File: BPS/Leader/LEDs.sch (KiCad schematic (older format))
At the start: 16 parts

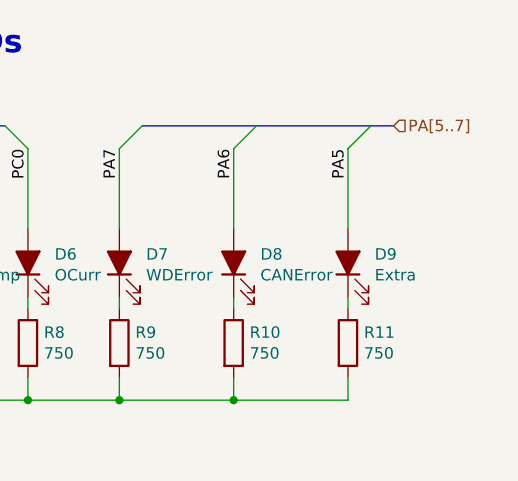
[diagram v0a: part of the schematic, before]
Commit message: Places most components of leader board in their respective locations with nothing traced
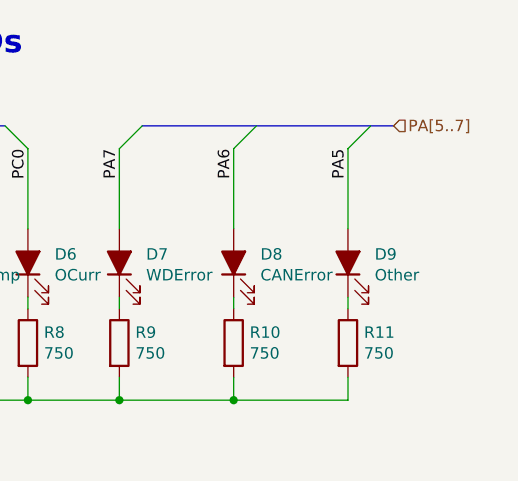
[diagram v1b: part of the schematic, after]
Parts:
- D9: value Extra -> Other
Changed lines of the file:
@@
 P 6300 3100
 F 0 "D9" V 6338 2983 50  0000 R CNN
-F 1 "Extra" V 6247 2983 50  0000 R CNN
+F 1 "Other" V 6247 2983 50  0000 R CNN
 F 2 "LED_SMD:LED_0805_2012Metric" H 6300 3100 50  0001 C CNN
 F 3 "~" H 6300 3100 50  0001 C CNN

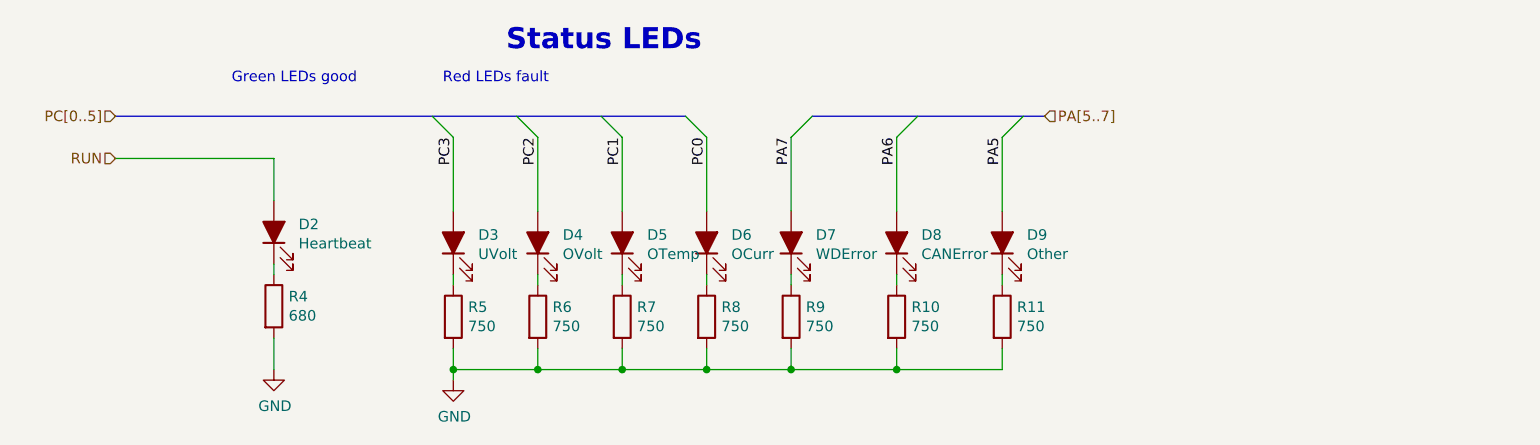
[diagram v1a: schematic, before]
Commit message: Adds power planes
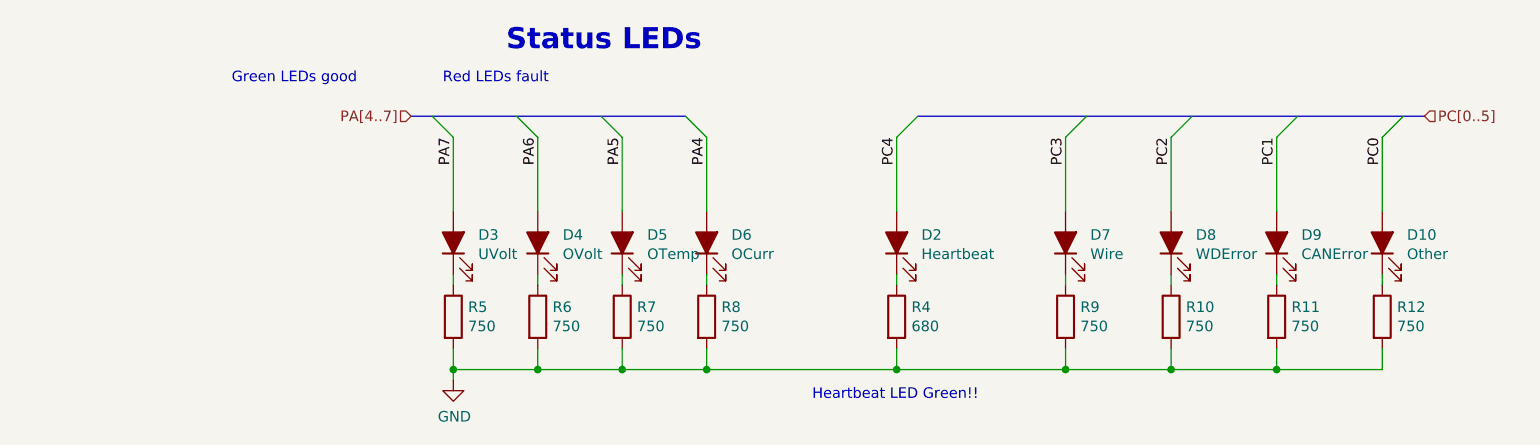
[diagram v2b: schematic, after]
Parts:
- added D10: Other, LED_SMD:LED_0805_2012Metric, symbol Device:LED_ALT
- added R12: 750, Resistor_SMD:R_0805_2012Metric, symbol Device:R
- D7: value WDError -> Wire
- D8: value CANError -> WDError
- D9: value Other -> CANError
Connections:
- net GND: now also R12.2
- net PA5: now also D5.2 (A); no longer D9.2 (A)
- net PA6: now also D4.2 (A); no longer D8.2 (A)
- net PA7: now also D3.2 (A); no longer D7.2 (A)
- net PC0: now also D10.2 (A); no longer D6.2 (A)
- net PC1: now also D9.2 (A); no longer D5.2 (A)
- net PC2: now also D8.2 (A); no longer D4.2 (A)
- net PC3: now also D7.2 (A); no longer D3.2 (A)
- net RUN renamed PC4
- new net: D10.1 (K), R12.1
- new net PA4: D6.2 (A)
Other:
- note added: "Heartbeat LED Green!!"
- moved on the sheet: D2, D7, D8, D9, R10, R11, R4, R9
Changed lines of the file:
@@
 Comment4 ""
 $EndDescr
-Text HLabel 2100 2500 0    50   Input ~ 0
+Text HLabel 8300 2500 2    50   Input ~ 0
 PC[0..5]
 $Comp
 L Device:LED_ALT D2
 U 1 1 5C3C069F
-P 2850 3050
-F 0 "D2" V 2888 2933 50  0000 R CNN
-F 1 "Heartbeat" V 2797 2933 50  0000 R CNN
-F 2 "LED_SMD:LED_0805_2012Metric" H 2850 3050 50  0001 C CNN
-F 3 "~" H 2850 3050 50  0001 C CNN
-F 4 "Green" V 2850 3050 50  0001 C CNN "Color"
-F 5 "APTD2012LCGCK" V 2850 3050 50  0001 C CNN "P/N"
-	1    2850 3050
+P 5800 3100
+F 0 "D2" V 5838 2983 50  0000 R CNN
+F 1 "Heartbeat" V 5747 2983 50  0000 R CNN
+F 2 "LED_SMD:LED_0805_2012Metric" H 5800 3100 50  0001 C CNN
+F 3 "~" H 5800 3100 50  0001 C CNN
+F 4 "Green" V 5800 3100 50  0001 C CNN "Color"
+F 5 "APTD2012LCGCK" V 5800 3100 50  0001 C CNN "P/N"
+	1    5800 3100
 	0    -1   -1   0
 $EndComp
@@
 	0    -1   -1   0
 $EndComp
-$Comp
-L power:GND #PWR033
-U 1 1 5C3C06CA
-P 2850 3700
-F 0 "#PWR033" H 2850 3450 50  0001 C CNN
-F 1 "GND" H 2855 3527 50  0000 C CNN
-F 2 "" H 2850 3700 50  0001 C CNN
-F 3 "" H 2850 3700 50  0001 C CNN
-	1    2850 3700
-	1    0    0    -1
-$EndComp
 Wire Wire Line
 	4900 3700 4900 3600
@@
 L Device:R R4
 U 1 1 5C3C06D9
-P 2850 3400
-F 0 "R4" H 2920 3446 50  0000 L CNN
-F 1 "680" H 2920 3355 50  0000 L CNN
-F 2 "Resistor_SMD:R_0805_2012Metric" V 2780 3400 50  0001 C CNN
-F 3 "~" H 2850 3400 50  0001 C CNN
-	1    2850 3400
+P 5800 3450
+F 0 "R4" H 5870 3496 50  0000 L CNN
+F 1 "680" H 5870 3405 50  0000 L CNN
+F 2 "Resistor_SMD:R_0805_2012Metric" V 5730 3450 50  0001 C CNN
+F 3 "~" H 5800 3450 50  0001 C CNN
+	1    5800 3450
 	1    0    0    -1
 $EndComp
@@
 	3700 3250 3700 3300
 Wire Wire Line
-	2850 3200 2850 3250
-Wire Wire Line
-	3700 2950 3700 2600
-Wire Wire Line
-	4100 2950 4100 2600
-Wire Wire Line
-	4500 2950 4500 2600
-Wire Wire Line
-	4900 2950 4900 2600
-Text Label 3700 2600 3    50   ~ 0
+	5800 3250 5800 3300
+Wire Wire Line
+	8100 2950 8100 2600
+Wire Wire Line
+	7600 2950 7600 2600
+Wire Wire Line
+	7100 2950 7100 2600
+Wire Wire Line
+	6600 2950 6600 2600
+Text Label 6600 2600 3    50   ~ 0
 PC3
-Text Label 4100 2600 3    50   ~ 0
+Text Label 7100 2600 3    50   ~ 0
 PC2
-Text Label 4500 2600 3    50   ~ 0
+Text Label 7600 2600 3    50   ~ 0
 PC1
-Text Label 4900 2600 3    50   ~ 0
+Text Label 8100 2600 3    50   ~ 0
 PC0
 Connection ~ 3700 3700
 Text Notes 2650 2350 0    50   ~ 0
 Green LEDs good
-$Comp
-L Device:LED_ALT D7
-U 1 1 5C3C070F
-P 5300 3100
-F 0 "D7" V 5338 2983 50  0000 R CNN
-F 1 "WDError" V 5247 2983 50  0000 R CNN
-F 2 "LED_SMD:LED_0805_2012Metric" H 5300 3100 50  0001 C CNN
-F 3 "~" H 5300 3100 50  0001 C CNN
-F 4 "Red" V 5300 3100 50  0001 C CNN "Color"
-F 5 "APTD2012LSURCK" V 5300 3100 50  0001 C CNN "P/N"
-	1    5300 3100
-	0    -1   -1   0
-$EndComp
-Wire Wire Line
-	5300 3700 5300 3600
-Wire Wire Line
-	4900 3700 5300 3700
+Wire Wire Line
+	6600 3700 6600 3600
 $Comp
 L Device:R R9
 U 1 1 5C3C0718
-P 5300 3450
-F 0 "R9" H 5370 3496 50  0000 L CNN
-F 1 "750" H 5370 3405 50  0000 L CNN
-F 2 "Resistor_SMD:R_0805_2012Metric" V 5230 3450 50  0001 C CNN
-F 3 "~" H 5300 3450 50  0001 C CNN
-	1    5300 3450
-	1    0    0    -1
-$EndComp
-Wire Wire Line
-	5300 3250 5300 3300
-Wire Wire Line
-	5300 2950 5300 2600
-Wire Wire Line
-	2850 3550 2850 3700
+P 6600 3450
+F 0 "R9" H 6670 3496 50  0000 L CNN
+F 1 "750" H 6670 3405 50  0000 L CNN
+F 2 "Resistor_SMD:R_0805_2012Metric" V 6530 3450 50  0001 C CNN
+F 3 "~" H 6600 3450 50  0001 C CNN
+	1    6600 3450
+	1    0    0    -1
+$EndComp
+Wire Wire Line
+	6600 3250 6600 3300
+Wire Wire Line
+	4900 2950 4900 2600
+Wire Wire Line
+	5800 3600 5800 3700
 $Comp
 L power:GND #PWR034
@@
 Text Notes 3650 2350 0    50   ~ 0
 Red LEDs fault
-Connection ~ 4900 3700
 Text Notes 3950 2200 0    100  ~ 20
 Status LEDs
 Entry Wire Line
-	3600 2500 3700 2600
-Entry Wire Line
-	4000 2500 4100 2600
-Entry Wire Line
-	4400 2500 4500 2600
-Entry Wire Line
-	4800 2500 4900 2600
+	8200 2500 8100 2600
+Entry Wire Line
+	7700 2500 7600 2600
+Entry Wire Line
+	7200 2500 7100 2600
+Entry Wire Line
+	6700 2500 6600 2600
+Wire Wire Line
+	7100 3700 7100 3600
+$Comp
+L Device:R R10
+U 1 1 5C6CF943
+P 7100 3450
+F 0 "R10" H 7170 3496 50  0000 L CNN
+F 1 "750" H 7170 3405 50  0000 L CNN
+F 2 "Resistor_SMD:R_0805_2012Metric" V 7030 3450 50  0001 C CNN
+F 3 "~" H 7100 3450 50  0001 C CNN
+	1    7100 3450
+	1    0    0    -1
+$EndComp
+Wire Wire Line
+	7100 3250 7100 3300
+Wire Wire Line
+	4500 2950 4500 2600
+Wire Wire Line
+	6600 3700 7100 3700
+Connection ~ 6600 3700
+Entry Wire Line
+	4900 2600 4800 2500
+Entry Wire Line
+	4500 2600 4400 2500
+Text Label 4500 2600 3    50   ~ 0
+PA5
+Text Label 4100 2600 3    50   ~ 0
+PA6
+Text HLabel 3500 2500 0    50   Input ~ 0
+PA[4..7]
+Wire Wire Line
+	7600 3700 7600 3600
+$Comp
+L Device:R R11
+U 1 1 5C585DC3
+P 7600 3450
+F 0 "R11" H 7670 3496 50  0000 L CNN
+F 1 "750" H 7670 3405 50  0000 L CNN
+F 2 "Resistor_SMD:R_0805_2012Metric" V 7530 3450 50  0001 C CNN
+F 3 "~" H 7600 3450 50  0001 C CNN
+	1    7600 3450
+	1    0    0    -1
+$EndComp
+Wire Wire Line
+	7600 3250 7600 3300
+Wire Wire Line
+	4100 2950 4100 2600
+Wire Wire Line
+	7100 3700 7600 3700
+Entry Wire Line
+	4100 2600 4000 2500
+Text Label 3700 2600 3    50   ~ 0
+PA7
+Wire Wire Line
+	5800 2950 5800 2600
+Connection ~ 7100 3700
+$Comp
+L Device:LED_ALT D10
+U 1 1 5F16CED0
+P 8100 3100
+F 0 "D10" V 8138 2983 50  0000 R CNN
+F 1 "Other" V 8047 2983 50  0000 R CNN
+F 2 "LED_SMD:LED_0805_2012Metric" H 8100 3100 50  0001 C CNN
+F 3 "~" H 8100 3100 50  0001 C CNN
+F 4 "Red" V 8100 3100 50  0001 C CNN "Color"
+F 5 "APTD2012LSURCK" V 8100 3100 50  0001 C CNN "P/N"
+	1    8100 3100
+	0    -1   -1   0
+$EndComp
+$Comp
+L Device:R R12
+U 1 1 5F16CED6
+P 8100 3450
+F 0 "R12" H 8170 3496 50  0000 L CNN
+F 1 "750" H 8170 3405 50  0000 L CNN
+F 2 "Resistor_SMD:R_0805_2012Metric" V 8030 3450 50  0001 C CNN
+F 3 "~" H 8100 3450 50  0001 C CNN
+	1    8100 3450
+	1    0    0    -1
+$EndComp
+Wire Wire Line
+	8100 3250 8100 3300
+Wire Wire Line
+	3700 2950 3700 2600
+Entry Wire Line
+	3700 2600 3600 2500
+Text Label 4900 2600 3    50   ~ 0
+PA4
+Wire Wire Line
+	8100 3700 8100 3600
+Connection ~ 7600 3700
+Wire Wire Line
+	7600 3700 8100 3700
+$Comp
+L Device:LED_ALT D7
+U 1 1 5C3C070F
+P 6600 3100
+F 0 "D7" V 6638 2983 50  0000 R CNN
+F 1 "Wire" V 6547 2983 50  0000 R CNN
+F 2 "LED_SMD:LED_0805_2012Metric" H 6600 3100 50  0001 C CNN
+F 3 "~" H 6600 3100 50  0001 C CNN
+F 4 "Red" V 6600 3100 50  0001 C CNN "Color"
+F 5 "APTD2012LSURCK" V 6600 3100 50  0001 C CNN "P/N"
+	1    6600 3100
+	0    -1   -1   0
+$EndComp
 $Comp
 L Device:LED_ALT D8
 U 1 1 5C6CF93B
-P 5800 3100
-F 0 "D8" V 5838 2983 50  0000 R CNN
-F 1 "CANError" V 5747 2983 50  0000 R CNN
-F 2 "LED_SMD:LED_0805_2012Metric" H 5800 3100 50  0001 C CNN
-F 3 "~" H 5800 3100 50  0001 C CNN
-F 4 "Red" V 5800 3100 50  0001 C CNN "Color"
-F 5 "APTD2012LSURCK" V 5800 3100 50  0001 C CNN "P/N"
-	1    5800 3100
-	0    -1   -1   0
-$EndComp
-Wire Wire Line
-	5800 3700 5800 3600
-$Comp
-L Device:R R10
-U 1 1 5C6CF943
-P 5800 3450
-F 0 "R10" H 5870 3496 50  0000 L CNN
-F 1 "750" H 5870 3405 50  0000 L CNN
-F 2 "Resistor_SMD:R_0805_2012Metric" V 5730 3450 50  0001 C CNN
-F 3 "~" H 5800 3450 50  0001 C CNN
-	1    5800 3450
-	1    0    0    -1
-$EndComp
-Wire Wire Line
-	5800 3250 5800 3300
-Wire Wire Line
-	5800 2950 5800 2600
-Wire Wire Line
-	5300 3700 5800 3700
-Connection ~ 5300 3700
-Entry Wire Line
-	5300 2600 5400 2500
-Entry Wire Line
-	5800 2600 5900 2500
-Text Label 6300 2600 3    50   ~ 0
-PA5
-Text Label 5800 2600 3    50   ~ 0
-PA6
-Text HLabel 6500 2500 2    50   Input ~ 0
-PA[5..7]
+P 7100 3100
+F 0 "D8" V 7138 2983 50  0000 R CNN
+F 1 "WDError" V 7047 2983 50  0000 R CNN
+F 2 "LED_SMD:LED_0805_2012Metric" H 7100 3100 50  0001 C CNN
+F 3 "~" H 7100 3100 50  0001 C CNN
+F 4 "Red" V 7100 3100 50  0001 C CNN "Color"
+F 5 "APTD2012LSURCK" V 7100 3100 50  0001 C CNN "P/N"
+	1    7100 3100
+	0    -1   -1   0
+$EndComp
 $Comp
 L Device:LED_ALT D9
 U 1 1 5C585DBB
-P 6300 3100
-F 0 "D9" V 6338 2983 50  0000 R CNN
-F 1 "Other" V 6247 2983 50  0000 R CNN
-F 2 "LED_SMD:LED_0805_2012Metric" H 6300 3100 50  0001 C CNN
-F 3 "~" H 6300 3100 50  0001 C CNN
-F 4 "Red" V 6300 3100 50  0001 C CNN "Color"
-F 5 "APTD2012LSURCK" V 6300 3100 50  0001 C CNN "P/N"
-	1    6300 3100
-	0    -1   -1   0
-$EndComp
-Wire Wire Line
-	6300 3700 6300 3600
-$Comp
-L Device:R R11
-U 1 1 5C585DC3
-P 6300 3450
-F 0 "R11" H 6370 3496 50  0000 L CNN
-F 1 "750" H 6370 3405 50  0000 L CNN
-F 2 "Resistor_SMD:R_0805_2012Metric" V 6230 3450 50  0001 C CNN
-F 3 "~" H 6300 3450 50  0001 C CNN
-	1    6300 3450
-	1    0    0    -1
-$EndComp
-Wire Wire Line
-	6300 3250 6300 3300
-Wire Wire Line
-	6300 2950 6300 2600
-Wire Wire Line
-	5800 3700 6300 3700
-Entry Wire Line
-	6300 2600 6400 2500
-Text Label 5300 2600 3    50   ~ 0
-PA7
-Wire Wire Line
-	2850 2900 2850 2700
-Wire Wire Line
-	2850 2700 2100 2700
-Text HLabel 2100 2700 0    50   Input ~ 0
-RUN
+P 7600 3100
+F 0 "D9" V 7638 2983 50  0000 R CNN
+F 1 "CANError" V 7547 2983 50  0000 R CNN
+F 2 "LED_SMD:LED_0805_2012Metric" H 7600 3100 50  0001 C CNN
+F 3 "~" H 7600 3100 50  0001 C CNN
+F 4 "Red" V 7600 3100 50  0001 C CNN "Color"
+F 5 "APTD2012LSURCK" V 7600 3100 50  0001 C CNN "P/N"
+	1    7600 3100
+	0    -1   -1   0
+$EndComp
+Wire Wire Line
+	4900 3700 5800 3700
+Connection ~ 4900 3700
 Connection ~ 5800 3700
+Wire Wire Line
+	5800 3700 6600 3700
 Wire Bus Line
-	5400 2500 6500 2500
+	3500 2500 4800 2500
 Wire Bus Line
-	2100 2500 4800 2500
+	5900 2500 8300 2500
+Entry Wire Line
+	5800 2600 5900 2500
+Text Label 5800 2600 3    50   ~ 0
+PC4
+Text Notes 5400 3850 0    50   ~ 0
+Heartbeat LED Green!!
 $EndSCHEMATC

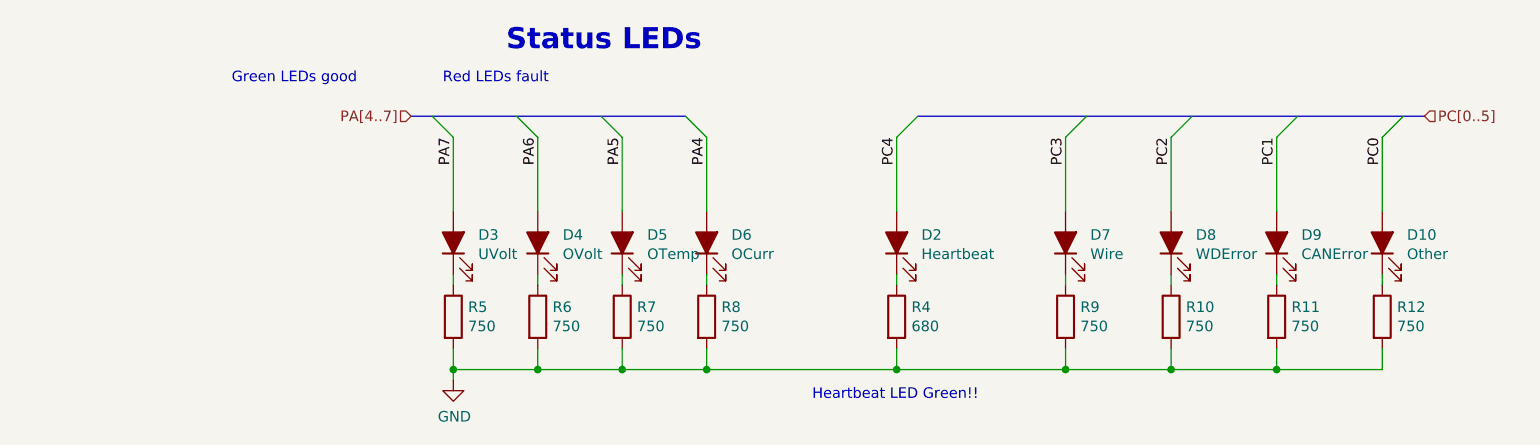
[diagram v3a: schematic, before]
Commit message: Simplifies dc-dc converter schematics
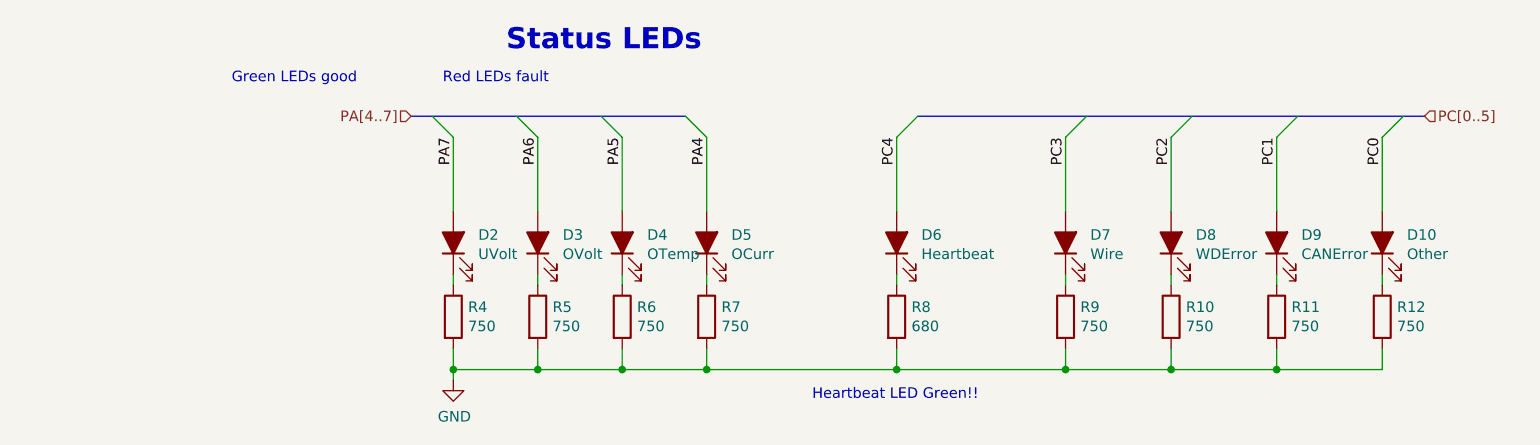
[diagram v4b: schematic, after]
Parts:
- renumbered D3 to D2, D4 to D3, D5 to D4, D6 to D5, D2 to D6, R5 to R4, R6 to R5, R7 to R6, R8 to R7, R4 to R8
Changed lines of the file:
@@
 PC[0..5]
 $Comp
-L Device:LED_ALT D2
+L Device:LED_ALT D6
 U 1 1 5C3C069F
 P 5800 3100
-F 0 "D2" V 5838 2983 50  0000 R CNN
+F 0 "D6" V 5838 2983 50  0000 R CNN
 F 1 "Heartbeat" V 5747 2983 50  0000 R CNN
 F 2 "LED_SMD:LED_0805_2012Metric" H 5800 3100 50  0001 C CNN
@@
 $EndComp
 $Comp
-L Device:LED_ALT D3
+L Device:LED_ALT D2
 U 1 1 5C3C06A8
 P 3700 3100
-F 0 "D3" V 3738 2982 50  0000 R CNN
+F 0 "D2" V 3738 2982 50  0000 R CNN
 F 1 "UVolt" V 3647 2982 50  0000 R CNN
 F 2 "LED_SMD:LED_0805_2012Metric" H 3700 3100 50  0001 C CNN
@@
 $EndComp
 $Comp
-L Device:LED_ALT D4
+L Device:LED_ALT D3
 U 1 1 5C3C06B1
 P 4100 3100
-F 0 "D4" V 4138 2982 50  0000 R CNN
+F 0 "D3" V 4138 2982 50  0000 R CNN
 F 1 "OVolt" V 4047 2982 50  0000 R CNN
 F 2 "LED_SMD:LED_0805_2012Metric" H 4100 3100 50  0001 C CNN
@@
 $EndComp
 $Comp
-L Device:LED_ALT D5
+L Device:LED_ALT D4
 U 1 1 5C3C06BA
 P 4500 3100
-F 0 "D5" V 4538 2982 50  0000 R CNN
+F 0 "D4" V 4538 2982 50  0000 R CNN
 F 1 "OTemp" V 4447 2982 50  0000 R CNN
 F 2 "LED_SMD:LED_0805_2012Metric" H 4500 3100 50  0001 C CNN
@@
 $EndComp
 $Comp
-L Device:LED_ALT D6
+L Device:LED_ALT D5
 U 1 1 5C3C06C3
 P 4900 3100
-F 0 "D6" V 4938 2983 50  0000 R CNN
+F 0 "D5" V 4938 2983 50  0000 R CNN
 F 1 "OCurr" V 4847 2983 50  0000 R CNN
 F 2 "LED_SMD:LED_0805_2012Metric" H 4900 3100 50  0001 C CNN
@@
 	3700 3700 4100 3700
 $Comp
-L Device:R R4
+L Device:R R8
 U 1 1 5C3C06D9
 P 5800 3450
-F 0 "R4" H 5870 3496 50  0000 L CNN
+F 0 "R8" H 5870 3496 50  0000 L CNN
 F 1 "680" H 5870 3405 50  0000 L CNN
 F 2 "Resistor_SMD:R_0805_2012Metric" V 5730 3450 50  0001 C CNN
@@
 $EndComp
 $Comp
-L Device:R R5
+L Device:R R4
 U 1 1 5C3C06E0
 P 3700 3450
-F 0 "R5" H 3770 3496 50  0000 L CNN
+F 0 "R4" H 3770 3496 50  0000 L CNN
 F 1 "750" H 3770 3405 50  0000 L CNN
 F 2 "Resistor_SMD:R_0805_2012Metric" V 3630 3450 50  0001 C CNN
@@
 $EndComp
 $Comp
-L Device:R R6
+L Device:R R5
 U 1 1 5C3C06E7
 P 4100 3450
-F 0 "R6" H 4170 3496 50  0000 L CNN
+F 0 "R5" H 4170 3496 50  0000 L CNN
 F 1 "750" H 4170 3405 50  0000 L CNN
 F 2 "Resistor_SMD:R_0805_2012Metric" V 4030 3450 50  0001 C CNN
@@
 $EndComp
 $Comp
-L Device:R R7
+L Device:R R6
 U 1 1 5C3C06EE
 P 4500 3450
-F 0 "R7" H 4570 3496 50  0000 L CNN
+F 0 "R6" H 4570 3496 50  0000 L CNN
 F 1 "750" H 4570 3405 50  0000 L CNN
 F 2 "Resistor_SMD:R_0805_2012Metric" V 4430 3450 50  0001 C CNN
@@
 $EndComp
 $Comp
-L Device:R R8
+L Device:R R7
 U 1 1 5C3C06F5
 P 4900 3450
-F 0 "R8" H 4970 3496 50  0000 L CNN
+F 0 "R7" H 4970 3496 50  0000 L CNN
 F 1 "750" H 4970 3405 50  0000 L CNN
 F 2 "Resistor_SMD:R_0805_2012Metric" V 4830 3450 50  0001 C CNN
@@
 	5800 3600 5800 3700
 $Comp
-L power:GND #PWR034
+L power:GND #PWR033
 U 1 1 5C3C0722
 P 3700 3750
-F 0 "#PWR034" H 3700 3500 50  0001 C CNN
+F 0 "#PWR033" H 3700 3500 50  0001 C CNN
 F 1 "GND" H 3705 3577 50  0000 C CNN
 F 2 "" H 3700 3750 50  0001 C CNN
